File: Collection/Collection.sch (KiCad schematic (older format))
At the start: 3 parts

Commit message: Added power supply schematics to collection.
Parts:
- added C? (x21): C, symbol Device:C
- added D? (x20): D, symbol Device:D
- added L?: FlyBack_Pri_9Winds, symbol Device:L_Core_Ferrite
- added L?: FlyBack_SEC_47Winds_220V, symbol Device:L_Core_Ferrite
- added L?: FlyBack_SEC_13Winds_-100V, symbol Device:L_Core_Ferrite
- added L?: FlyBack_Pri_2-3Winds_6.3VRMS, symbol Device:L_Core_Ferrite
- added L?: FlyBack_Pri_1600Winds_Anode_8-12KV, symbol Device:L_Core_Ferrite
- added L? (x2): Pri_20Winds, symbol Device:L_Core_Ferrite
- added L? (x2): Sec_40Winds, symbol Device:L_Core_Ferrite
- added NE?: Lamp_Neon, symbol Device:Lamp_Neon
- added Q? (x9): Q_NPN, symbol Device:Q_NPN_BCE
- added Q? (x6): Q_PNP, symbol Device:Q_PNP_BCE
- added Q? (x3): Q_NMOS_200V, symbol Device:Q_NMOS_DGS
- added R? (x30): R, symbol Device:R
- added RV? (x3): R_POT, symbol Device:R_POT
- added U1A, U1A?, U1B, U1B?, U1C, U1C?, U1D, U1D?: OPAMP, symbol pspice:OPAMP
- added U? (x2): L7805, symbol Regulator_Linear:L7805
- added U?: 74LS74, symbol 74xx:74LS74
- added U? (x2): 74LS00, symbol 74xx:74LS00
- added U?: L7905, symbol Regulator_Linear:L7905
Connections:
- net +5V: now also C?.1, C?.1, C?.1, C?.1, R?.1, R?.1, R?.1, R?.1, RV?.1, RV?.1, U1A.4 (V+), U1A?.4 (V+), U1B.4 (V+), U1B?.4 (V+), U1C.4 (V+), U1C?.4 (V+), U1D.4 (V+), U1D?.4 (V+), U?.1 (~R), U?.3 (OUT), U?.3 (OUT), U?.4 (~S)
- net CE0 renamed RPI_CE0
- net CE1 renamed RPI_CE1
- net IntensityDAC renamed Intensity_DAC_CE
- net XYdax renamed XY_DAC_CE
- new net: R?.2, R?.2, U1A.2 (-)
- new net: R?.1, R?.2, U1A.3
- new net: D?.1 (K), D?.1 (K), R?.2, U1C.1 (+)
- new net: C?.2, R?.1, U1B.3, U1C.2 (-)
- new net: R?.2, U1C.3
- new net: R?.1, R?.2, U1D.1 (+)
- new net: RV?.2, U1D.2 (-)
- new net: D?.2 (A), U1D.3
- new net: C?.1, R?.1, U1B.2 (-)
- new net: C?.2, D?.2 (A), R?.1, R?.2 (x2)
- new net: Q?.1 (B), R?.1 (x3)
- new net: Q?.1 (B), Q?.1 (B), Q?.2 (C), R?.2 (x3)
- new net: Q?.1 (B), Q?.1 (B), Q?.2 (C), Q?.3 (E) (x3)
- new net: Q?.2 (C), Q?.3 (E), R?.2 (x3)
- new net: L?.2, Q?.1 (D) (x2)
- new net: Q?.2 (G), R?.1 (x3)
- new net: D?.1 (K), D?.2 (A), L?.1, L?.2
- new net: D?.2 (A), L?.1 (x2)
- new net: D?.1 (K), D?.2 (A) (x11)
- new net: C?.1, C?.2
- new net: R?.2, R?.2, U1A?.2 (-)
- new net: R?.1, R?.2, U1A?.3
- new net: C?.2, R?.1, U1B?.3, U1C?.1 (+)
- new net: D?.1 (K), D?.1 (K), R?.2, U1C?.2 (-)
- new net: U1C?.3, U?.1, U?.3 (C), U?.5
- new net: R?.1, R?.2, U1D?.1 (+)
- new net: RV?.2, U1D?.2 (-)
- new net: D?.2 (A), U1D?.3
- new net: C?.1, R?.1, U1B?.2 (-)
- new net: U?.2 (D), U?.4, U?.6 (~Q)
- new net: U?.2, U?.5 (Q)
- new net: R?.2, U?.3
- new net: L?.1, Q?.1 (D)
- new net: R?.2, U?.6
- new net: D?.1 (K), L?.1
- new net +12V: C?.1, C?.1, C?.1, C?.1, L?.1, L?.1, L?.2, Q?.2 (C), Q?.2 (C), Q?.2 (C), Q?.2 (C), Q?.2 (C), Q?.2 (C), R?.1, R?.1, R?.1, U?.1 (IN), U?.1 (IN)
- new net +25V: C?.1, D?.1 (K), R?.1
- new net +2V5: C?.1, C?.1, R?.1, R?.1, R?.2, R?.2, U1A.1 (+), U1A?.1 (+), U1B.1 (+), U1B?.1 (+)
- new net -100V: C?.1, D?.2 (A), R?.2
- new net -25V: C?.1, C?.2, D?.2 (A), U?.2 (VI)
- new net -5V: C?.2, U?.3 (VO)
- new net CRT+220V: C?.1, D?.1 (K), R?.1
- new net CRT_ANODE_8-12KV: C?.1, D?.1 (K)
- new net CRT_GRID: C?.1, NE?.2, R?.1, RV?.1, RV?.2
- new net CRT_Heater2: L?.1
- new net GND: C?.1, C?.1, C?.2, C?.2, C?.2, C?.2, C?.2, C?.2, C?.2, C?.2, C?.2, C?.2, C?.2, C?.2, C?.2, C?.2, L?.1, L?.2, L?.2, L?.2, L?.2, L?.2, NE?.1, Q?.3 (E), Q?.3 (E), Q?.3 (E), Q?.3 (E), Q?.3 (E), Q?.3 (E), Q?.3 (E), Q?.3 (E), Q?.3 (E), Q?.3 (S), Q?.3 (S), Q?.3 (S), R?.1, R?.1, R?.2, R?.2, R?.2, R?.2, R?.2, R?.2, RV?.3, RV?.3, U1A.5 (V-), U1A?.5 (V-), U1B.5 (V-), U1B?.5 (V-), U1C.5 (V-), U1C?.5 (V-), U1D.5 (V-), U1D?.5 (V-), U?.1 (GND), U?.2 (GND), U?.2 (GND)
- new net IntensityCTRL: RV?.3
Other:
- moved on the sheet: U?A, U?B

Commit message: Added Deflection Amp Schematic and Beam Intensity Control Schematic.
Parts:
- added C? (x3): C, symbol Device:C
- added D? (x4): D, symbol Device:D
- added D?: LED, symbol Device:LED
- added L?: X_Deflection, symbol Device:L_Core_Ferrite
- added L?: Y_Deflection, symbol Device:L_Core_Ferrite
- added Q?: Q_PNP_100V, symbol Device:Q_PNP_BCE
- added R? (x17): R, symbol Device:R
- added RV? (x8): R_POT, symbol Device:R_POT
- added U1D? (x6): LM741, symbol pspice:OPAMP
- added U1D? (x2): OPAMP, symbol pspice:OPAMP
- added U? (x2): EL817, Package_DIP:DIP-4_W7.62mm, symbol Isolator:EL817
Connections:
- net +25V: now also U1D?.4 (V+), U1D?.4 (V+)
- net +5V: no longer C?.1, C?.1, R?.1, R?.1, U1A?.4 (V+), U1B?.4 (V+), U1C?.4 (V+), U1D?.4 (V+), U?.3 (OUT), U?.4 (~S)
- net -25V: now also U1D?.5 (V-), U1D?.5 (V-)
- net -5V: now also R?.2, R?.2, U1D?.5 (V-), U1D?.5 (V-), U1D?.5 (V-), U1D?.5 (V-), U1D?.5 (V-), U1D?.5 (V-)
- net GND: now also C?.1, D?.1 (K), L?.2, L?.2, R?.1, R?.1, R?.1, R?.1, R?.1, R?.1, U1D?.2 (-), U1D?.2 (-), U?.1, U?.2, U?.3
- net IntensityCTRL: now also Q?.2 (C)
- new net: R?.2, RV?.3, U1D?.2 (-) (x6)
- new net: C?.1, R?.2, U1D?.1 (+) (x2)
- new net: L?.1, RV?.1, RV?.2, U1D?.3 (x2)
- new net: D?.2 (A), R?.1, RV?.1, RV?.2, U1D?.3 (x2)
- new net: R?.1, R?.2, U1D?.1 (+) (x2)
- new net: D?.2 (A), R?.2, U1D?.3 (x2)
- new net: C?.2, D?.1 (K), D?.1 (K), D?.1 (K), D?.1 (K), RV?.1, RV?.2
- new net: D?.2 (A), R?.2
- new net: R?.1, R?.1, RV?.3
- new net: R?.2, U?.1
- new net: U?.3, U?.4
- new net: Q?.3 (E), U?.4
- new net: R?.1, U?.2
- new net: Q?.1 (B), RV?.2
- new net: R?.1, RV?.3
- new net: R?.1, RV?.1
- new net +5VA: C?.1, C?.1, R?.1, R?.1, U1A?.4 (V+), U1B?.4 (V+), U1C?.4 (V+), U1D?.4 (V+), U1D?.4 (V+), U1D?.4 (V+), U1D?.4 (V+), U1D?.4 (V+), U1D?.4 (V+), U1D?.4 (V+), U?.3 (OUT), U?.4 (~S)
- new net Intensity_From_DAC: R?.2
- new net X_IN: U1D?.1 (+)
- new net X_SIGNAL: C?.2, R?.1, RV?.1, RV?.2, U1D?.1 (+), U1D?.3
- new net Y_IN: U1D?.1 (+)
- new net Y_SIGNAL: C?.2, R?.1, RV?.1, RV?.2, U1D?.1 (+), U1D?.3

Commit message: Updated Op-Amp types on schematics.
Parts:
- added C? (x2): C, symbol Device:C
- added R? (x2): R, symbol Device:R
- U1A, U1A?, U1B, U1B?, U1C, U1C?, U1D, U1D?: value OPAMP -> AD8668
- U1D? (x2): value OPAMP -> LM1875
- U1D? (x4): value LM741 -> LM324
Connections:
- net GND: now also R?.1, R?.1
- net X_SIGNAL: now also C?.2; no longer U1D?.1 (+)
- net Y_SIGNAL: now also C?.2; no longer U1D?.1 (+)
- new net: C?.1, R?.2, U1D?.1 (+) (x2)
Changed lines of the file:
@@
 P 9150 2750
 F 0 "U1A" H 9200 3000 50  0000 L CNN
-F 1 "OPAMP" H 9200 2900 50  0000 L CNN
+F 1 "AD8668" H 9200 2900 50  0000 L CNN
 F 2 "" H 9150 2750 50  0001 C CNN
 F 3 "~" H 9150 2750 50  0001 C CNN
@@
 P 11600 2750
 F 0 "U1C" H 11700 3000 50  0000 L CNN
-F 1 "OPAMP" H 11750 2900 50  0000 L CNN
+F 1 "AD8668" H 11650 2900 50  0000 L CNN
 F 2 "" H 11600 2750 50  0001 C CNN
 F 3 "~" H 11600 2750 50  0001 C CNN
@@
 P 10500 3750
 F 0 "U1D" H 10600 3900 50  0000 L CNN
-F 1 "OPAMP" H 10700 3700 50  0000 L CNN
+F 1 "AD8668" H 10700 3700 50  0000 L CNN
 F 2 "" H 10500 3750 50  0001 C CNN
 F 3 "~" H 10500 3750 50  0001 C CNN
@@
 P 10500 2650
 F 0 "U1B" H 10550 2850 50  0000 L CNN
-F 1 "OPAMP" H 10700 2800 50  0000 L CNN
+F 1 "AD8668" H 10700 2800 50  0000 L CNN
 F 2 "" H 10500 2650 50  0001 C CNN
 F 3 "~" H 10500 2650 50  0001 C CNN
@@
 P 3950 1500
 F 0 "U1B?" H 4000 1700 50  0000 L CNN
-F 1 "OPAMP" H 4150 1650 50  0000 L CNN
+F 1 "AD8668" H 4150 1650 50  0000 L CNN
 F 2 "" H 3950 1500 50  0001 C CNN
 F 3 "~" H 3950 1500 50  0001 C CNN
@@
 P 3950 2600
 F 0 "U1D?" H 4050 2750 50  0000 L CNN
-F 1 "OPAMP" H 4150 2550 50  0000 L CNN
+F 1 "AD8668" H 4150 2550 50  0000 L CNN
 F 2 "" H 3950 2600 50  0001 C CNN
 F 3 "~" H 3950 2600 50  0001 C CNN
@@
 P 5050 1600
 F 0 "U1C?" H 5150 1850 50  0000 L CNN
-F 1 "OPAMP" H 5200 1750 50  0000 L CNN
+F 1 "AD8668" H 5200 1750 50  0000 L CNN
 F 2 "" H 5050 1600 50  0001 C CNN
 F 3 "~" H 5050 1600 50  0001 C CNN
@@
 P 2600 1600
 F 0 "U1A?" H 2650 1850 50  0000 L CNN
-F 1 "OPAMP" H 2650 1750 50  0000 L CNN
+F 1 "AD8668" H 2650 1750 50  0000 L CNN
 F 2 "" H 2600 1600 50  0001 C CNN
 F 3 "~" H 2600 1600 50  0001 C CNN
@@
 P 3400 7900
 F 0 "U1D?" H 3500 8050 50  0000 L CNN
-F 1 "OPAMP" H 3600 7850 50  0000 L CNN
+F 1 "LM1875" H 3500 8150 50  0000 L CNN
 F 2 "" H 3400 7900 50  0001 C CNN
 F 3 "~" H 3400 7900 50  0001 C CNN
@@
 P 3400 9600
 F 0 "U1D?" H 3500 9750 50  0000 L CNN
-F 1 "OPAMP" H 3600 9550 50  0000 L CNN
+F 1 "LM1875" H 3450 9850 50  0000 L CNN
 F 2 "" H 3400 9600 50  0001 C CNN
 F 3 "~" H 3400 9600 50  0001 C CNN
@@
 P 6000 7850
 F 0 "U1D?" H 6100 8000 50  0000 L CNN
-F 1 "LM741" H 6000 8100 50  0000 L CNN
+F 1 "LM324" H 6000 8100 50  0000 L CNN
 F 2 "" H 6000 7850 50  0001 C CNN
 F 3 "~" H 6000 7850 50  0001 C CNN
@@
 P 6000 9550
 F 0 "U1D?" H 6100 9700 50  0000 L CNN
-F 1 "LM741" H 6050 9800 50  0000 L CNN
+F 1 "LM324" H 6050 9800 50  0000 L CNN
 F 2 "" H 6000 9550 50  0001 C CNN
 F 3 "~" H 6000 9550 50  0001 C CNN
@@
 P 7250 7950
 F 0 "U1D?" H 7350 8100 50  0000 L CNN
-F 1 "LM741" H 7250 8200 50  0000 L CNN
+F 1 "LM324" H 7250 8200 50  0000 L CNN
 F 2 "" H 7250 7950 50  0001 C CNN
 F 3 "~" H 7250 7950 50  0001 C CNN
@@
 P 7250 9650
 F 0 "U1D?" H 7350 9800 50  0000 L CNN
-F 1 "LM741" H 7250 9900 50  0000 L CNN
+F 1 "LM324" H 7250 9900 50  0000 L CNN
 F 2 "" H 7250 9650 50  0001 C CNN
 F 3 "~" H 7250 9650 50  0001 C CNN
@@
 Text GLabel 8450 7250 0    50   Input ~ 0
 Intensity_Control
-Text Label 5200 7650 0    50   ~ 0
+Text Label 5200 7350 0    50   ~ 0
 X_SIGNAL
-Text Label 5200 9350 0    50   ~ 0
+Text Label 5200 9050 0    50   ~ 0
 Y_SIGNAL
+$Comp
+L Device:C C?
+U 1 1 643A120E
+P 5350 7750
+F 0 "C?" V 5050 7750 50  0000 C CNN
+F 1 "C" V 5150 7750 50  0000 C CNN
+F 2 "" H 5388 7600 50  0001 C CNN
+F 3 "~" H 5350 7750 50  0001 C CNN
+	1    5350 7750
+	0    1    1    0
+$EndComp
+$Comp
+L Device:C C?
+U 1 1 643A1B0E
+P 5350 9450
+F 0 "C?" V 5050 9450 50  0000 C CNN
+F 1 "C" V 5150 9450 50  0000 C CNN
+F 2 "" H 5388 9300 50  0001 C CNN
+F 3 "~" H 5350 9450 50  0001 C CNN
+	1    5350 9450
+	0    1    1    0
+$EndComp
+Wire Wire Line
+	5200 7350 5200 7750
+Wire Wire Line
+	5500 7750 5700 7750
 Wire Wire Line
-	5200 7750 5200 7650
+	5200 9050 5200 9450
 Wire Wire Line
-	5200 7750 5700 7750
+	5500 9450 5700 9450
+$Comp
+L Device:R R?
+U 1 1 6440C003
+P 5500 8100
+F 0 "R?" H 5400 8050 50  0000 R CNN
+F 1 "R" H 5400 8100 50  0000 R CNN
+F 2 "" V 5430 8100 50  0001 C CNN
+F 3 "~" H 5500 8100 50  0001 C CNN
+	1    5500 8100
+	-1   0    0    1
+$EndComp
+$Comp
+L power:GND #PWR?
+U 1 1 6440D5EB
+P 5500 8250
+F 0 "#PWR?" H 5500 8000 50  0001 C CNN
+F 1 "GND" H 5550 8050 50  0000 C CNN
+F 2 "" H 5500 8250 50  0001 C CNN
+F 3 "" H 5500 8250 50  0001 C CNN
+	1    5500 8250
+	1    0    0    -1
+$EndComp
+$Comp
+L Device:R R?
+U 1 1 64426FB5
+P 5500 9800
+F 0 "R?" H 5400 9750 50  0000 R CNN
+F 1 "R" H 5400 9800 50  0000 R CNN
+F 2 "" V 5430 9800 50  0001 C CNN
+F 3 "~" H 5500 9800 50  0001 C CNN
+	1    5500 9800
+	-1   0    0    1
+$EndComp
+$Comp
+L power:GND #PWR?
+U 1 1 644285B9
+P 5500 9950
+F 0 "#PWR?" H 5500 9700 50  0001 C CNN
+F 1 "GND" H 5550 9750 50  0000 C CNN
+F 2 "" H 5500 9950 50  0001 C CNN
+F 3 "" H 5500 9950 50  0001 C CNN
+	1    5500 9950
+	1    0    0    -1
+$EndComp
 Wire Wire Line
-	5200 9450 5200 9350
+	5500 9650 5500 9450
+Connection ~ 5500 9450
 Wire Wire Line
-	5200 9450 5700 9450
+	5500 7950 5500 7750
+Connection ~ 5500 7750
 $EndSCHEMATC

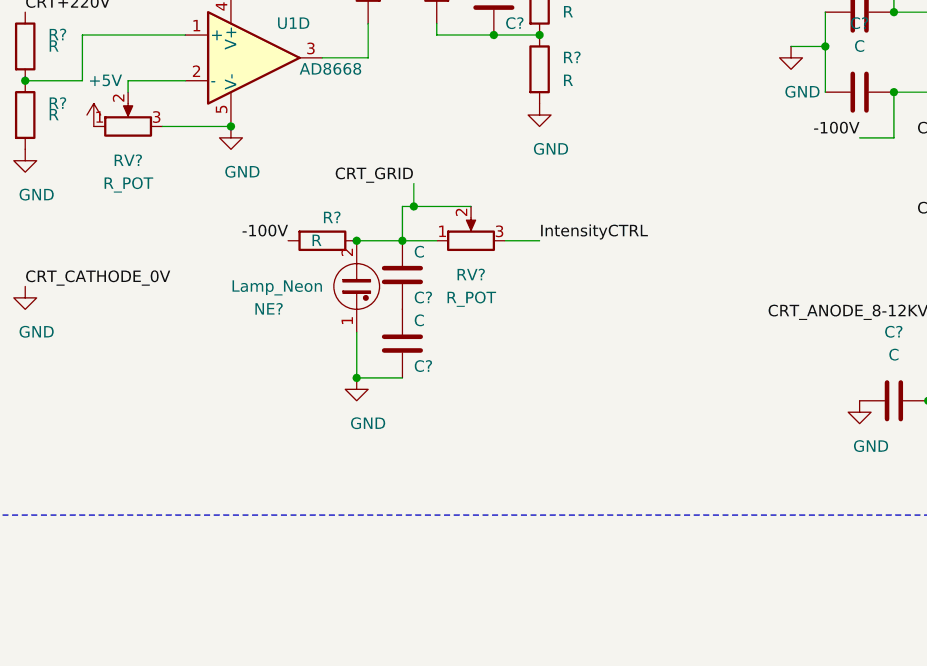
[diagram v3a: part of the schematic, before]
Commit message: Updated Intensity control Circuit.
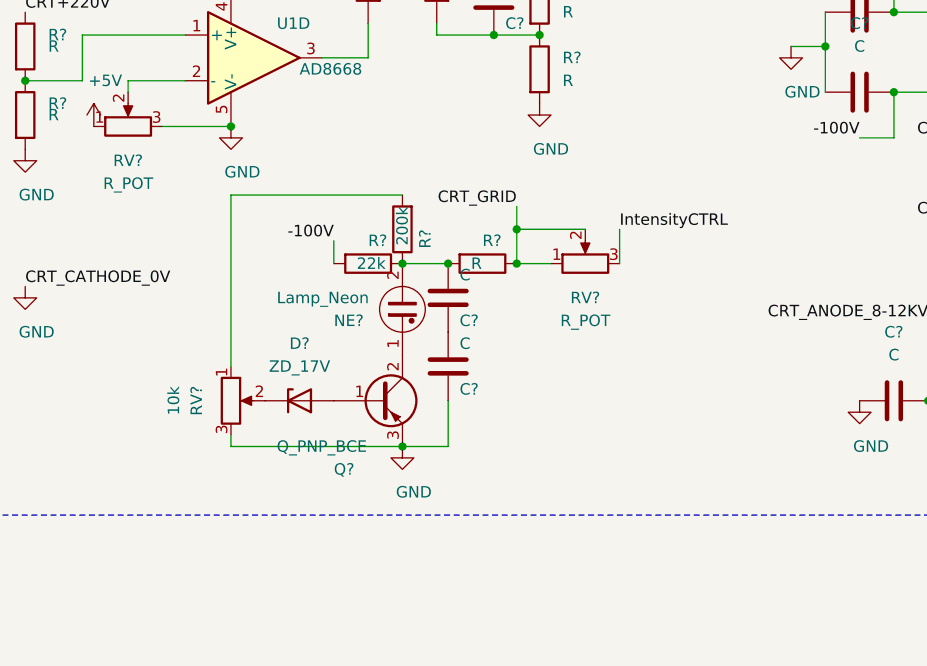
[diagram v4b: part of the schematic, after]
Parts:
- added D?: ZD_17V, symbol Device:D_Zener
- added Q?: Q_PNP_BCE, symbol Device:Q_PNP_BCE
- added R?: R, symbol Device:R
- added R?: 200k, symbol Device:R
- added RV?: 10k, symbol Device:R_POT
- R?: value R -> 22k
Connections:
- net CRT_GRID: now also R?.1; no longer C?.1, NE?.2, R?.1
- net GND: now also Q?.3 (E), RV?.3; no longer NE?.1
- new net: C?.1, NE?.2, R?.1, R?.1, R?.2
- new net: NE?.1, Q?.2 (C)
- new net: D?.2 (A), Q?.1 (B)
- new net: D?.1 (K), RV?.2
- new net: R?.2, RV?.1
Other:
- moved on the sheet: C?, NE?, R?, RV?
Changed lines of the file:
@@
 Wire Wire Line
 	14650 2400 14750 2400
-Text Label 10650 4550 2    50   ~ 0
+Text Label 10850 4550 2    50   ~ 0
 -100V
 $Comp
 L Device:Lamp_Neon NE?
 U 1 1 64460D5E
-P 10950 4750
-F 0 "NE?" H 10500 4650 50  0000 L CNN
-F 1 "Lamp_Neon" H 10400 4750 50  0000 L CNN
-F 2 "" V 10950 4850 50  0001 C CNN
-F 3 "~" V 10950 4850 50  0001 C CNN
-	1    10950 4750
+P 11150 4850
+F 0 "NE?" H 10850 4800 50  0000 L CNN
+F 1 "Lamp_Neon" H 10600 4900 50  0000 L CNN
+F 2 "" V 11150 4950 50  0001 C CNN
+F 3 "~" V 11150 4950 50  0001 C CNN
+	1    11150 4850
 	1    0    0    -1
 $EndComp
@@
 L Device:R R?
 U 1 1 644615DC
-P 10800 4550
-F 0 "R?" V 10700 4550 50  0000 L CNN
-F 1 "R" V 10800 4500 50  0000 L CNN
-F 2 "" V 10730 4550 50  0001 C CNN
-F 3 "~" H 10800 4550 50  0001 C CNN
-	1    10800 4550
+P 11000 4650
+F 0 "R?" V 10900 4650 50  0000 L CNN
+F 1 "22k" V 11000 4600 50  0000 L CNN
+F 2 "" V 10930 4650 50  0001 C CNN
+F 3 "~" H 11000 4650 50  0001 C CNN
+	1    11000 4650
 	0    1    1    0
 $EndComp
@@
 L power:GND #PWR?
 U 1 1 644620C7
-P 10950 5150
-F 0 "#PWR?" H 10950 4900 50  0001 C CNN
-F 1 "GND" H 11000 4950 50  0000 C CNN
-F 2 "" H 10950 5150 50  0001 C CNN
-F 3 "" H 10950 5150 50  0001 C CNN
-	1    10950 5150
+P 11150 5450
+F 0 "#PWR?" H 11150 5200 50  0001 C CNN
+F 1 "GND" H 11200 5250 50  0000 C CNN
+F 2 "" H 11150 5450 50  0001 C CNN
+F 3 "" H 11150 5450 50  0001 C CNN
+	1    11150 5450
 	1    0    0    -1
 $EndComp
@@
 L Device:C C?
 U 1 1 64462CFE
-P 11150 4700
-F 0 "C?" H 11200 4600 50  0000 L CNN
-F 1 "C" H 11200 4800 50  0000 L CNN
-F 2 "" H 11188 4550 50  0001 C CNN
-F 3 "~" H 11150 4700 50  0001 C CNN
-	1    11150 4700
+P 11350 4800
+F 0 "C?" H 11400 4700 50  0000 L CNN
+F 1 "C" H 11400 4900 50  0000 L CNN
+F 2 "" H 11388 4650 50  0001 C CNN
+F 3 "~" H 11350 4800 50  0001 C CNN
+	1    11350 4800
 	1    0    0    -1
 $EndComp
@@
 L Device:C C?
 U 1 1 6446347D
-P 11150 5000
-F 0 "C?" H 11200 4900 50  0000 L CNN
-F 1 "C" H 11200 5100 50  0000 L CNN
-F 2 "" H 11188 4850 50  0001 C CNN
-F 3 "~" H 11150 5000 50  0001 C CNN
-	1    11150 5000
-	1    0    0    -1
-$EndComp
-Wire Wire Line
-	11150 5150 10950 5150
-Wire Wire Line
-	10950 5150 10950 4950
-Connection ~ 10950 5150
-Wire Wire Line
-	10950 4550 11150 4550
-Connection ~ 10950 4550
+P 11350 5100
+F 0 "C?" H 11400 5000 50  0000 L CNN
+F 1 "C" H 11400 5200 50  0000 L CNN
+F 2 "" H 11388 4950 50  0001 C CNN
+F 3 "~" H 11350 5100 50  0001 C CNN
+	1    11350 5100
+	1    0    0    -1
+$EndComp
+Wire Wire Line
+	11150 4650 11350 4650
 $Comp
 L Device:R_POT RV?
 U 1 1 6446BA10
-P 11450 4550
-F 0 "RV?" V 11300 4550 50  0000 C CNN
-F 1 "R_POT" V 11200 4550 50  0000 C CNN
-F 2 "" H 11450 4550 50  0001 C CNN
-F 3 "~" H 11450 4550 50  0001 C CNN
-	1    11450 4550
+P 11950 4650
+F 0 "RV?" V 11800 4650 50  0000 C CNN
+F 1 "R_POT" V 11700 4650 50  0000 C CNN
+F 2 "" H 11950 4650 50  0001 C CNN
+F 3 "~" H 11950 4650 50  0001 C CNN
+	1    11950 4650
 	0    -1   -1   0
 $EndComp
 Wire Wire Line
-	11300 4550 11150 4550
-Connection ~ 11150 4550
-Wire Wire Line
-	11150 4550 11150 4400
-Wire Wire Line
-	11150 4400 11200 4400
-Text Label 11200 4300 2    50   ~ 0
+	11800 4650 11650 4650
+Connection ~ 11350 4650
+Text Label 11650 4400 2    50   ~ 0
 CRT_GRID
-Wire Wire Line
-	11200 4300 11200 4400
-Connection ~ 11200 4400
-Wire Wire Line
-	11200 4400 11450 4400
-Text Label 11750 4550 0    50   ~ 0
-IntensityCTRL
-Wire Wire Line
-	11750 4550 11600 4550
 Wire Notes Line
 	15600 5750 7950 5750
@@
 	5500 7950 5500 7750
 Connection ~ 5500 7750
+Text Label 12100 4500 0    50   ~ 0
+IntensityCTRL
+$Comp
+L Device:R R?
+U 1 1 6442BE8E
+P 11500 4650
+F 0 "R?" V 11400 4650 50  0000 L CNN
+F 1 "R" V 11500 4600 50  0000 L CNN
+F 2 "" V 11430 4650 50  0001 C CNN
+F 3 "~" H 11500 4650 50  0001 C CNN
+	1    11500 4650
+	0    1    1    0
+$EndComp
+Wire Wire Line
+	11650 4500 11650 4650
+Wire Wire Line
+	11650 4500 11950 4500
+Connection ~ 11650 4650
+Wire Wire Line
+	11650 4400 11650 4500
+Connection ~ 11650 4500
+Wire Wire Line
+	12100 4500 12100 4650
+$Comp
+L Device:Q_PNP_BCE Q?
+U 1 1 64495F1E
+P 11050 5250
+F 0 "Q?" H 10850 4950 50  0000 L CNN
+F 1 "Q_PNP_BCE" H 10600 5050 50  0000 L CNN
+F 2 "" H 11250 5350 50  0001 C CNN
+F 3 "~" H 11050 5250 50  0001 C CNN
+	1    11050 5250
+	1    0    0    -1
+$EndComp
+Connection ~ 11150 4650
+Wire Wire Line
+	11350 5250 11350 5450
+Wire Wire Line
+	11350 5450 11150 5450
+Connection ~ 11150 5450
+$Comp
+L Device:D_Zener D?
+U 1 1 644B4D2D
+P 10700 5250
+F 0 "D?" H 10700 5500 50  0000 C CNN
+F 1 "ZD_17V" H 10700 5400 50  0000 C CNN
+F 2 "" H 10700 5250 50  0001 C CNN
+F 3 "~" H 10700 5250 50  0001 C CNN
+	1    10700 5250
+	1    0    0    -1
+$EndComp
+Wire Wire Line
+	10850 4550 10850 4650
+$Comp
+L Device:R R?
+U 1 1 644EEF86
+P 11150 4500
+F 0 "R?" V 11050 4500 50  0000 L CNN
+F 1 "200k" V 11150 4400 50  0000 L CNN
+F 2 "" V 11080 4500 50  0001 C CNN
+F 3 "~" H 11150 4500 50  0001 C CNN
+	1    11150 4500
+	-1   0    0    1
+$EndComp
+$Comp
+L Device:R_POT RV?
+U 1 1 644F0E02
+P 10400 5250
+F 0 "RV?" V 10250 5250 50  0000 C CNN
+F 1 "10k" V 10150 5250 50  0000 C CNN
+F 2 "" H 10400 5250 50  0001 C CNN
+F 3 "~" H 10400 5250 50  0001 C CNN
+	1    10400 5250
+	1    0    0    -1
+$EndComp
+Wire Wire Line
+	11150 5450 10400 5450
+Wire Wire Line
+	10400 5450 10400 5400
+Wire Wire Line
+	10400 5100 10400 4350
+Wire Wire Line
+	10400 4350 11150 4350
 $EndSCHEMATC

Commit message: Updated schematic. Resistors values are NOT all correct yet.
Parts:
- removed R? (x48): R, symbol Device:R
- added R? (x47): 10K, Resistors_SMD:R_0603, symbol Device:R
- added R?: 870K, Resistors_SMD:R_0603, symbol Device:R
- R?: value R -> 180K; footprint (none) -> Resistors_SMD:R_0603
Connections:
- net +12V: now also R?.1, R?.1, R?.1
- net +2V5: now also R?.1, R?.1, R?.2, R?.2
- net +5V: now also R?.1, R?.1
- net +5VA: now also R?.1, R?.1
- net -5V: now also R?.2, R?.2
- net CRT+220V: now also R?.1
- net CRT_GRID: now also R?.2
- net GND: now also R?.1, R?.1, R?.2, R?.2, R?.2, R?.2, R?.2, R?.2, R?.2, R?.2, R?.2, R?.2, R?.2, R?.2, R?.2, R?.2
- net Intensity_From_DAC: now also R?.2
- net X_SIGNAL: now also R?.1
- net Y_SIGNAL: now also R?.1
- net at U1A.2 (-): now also R?.1, R?.2
- net at U1A.3: now also R?.1, R?.1
- net at D?.1 (K), D?.1 (K), U1C.1 (+): now also R?.2
- net at C?.2, U1B.3, U1C.2 (-): now also R?.2
- net at U1C.3: now also R?.1
- net at U1D.1 (+): now also R?.1, R?.2
- net at C?.1, U1B.2 (-): now also R?.2
- net at C?.2, D?.2 (A): now also R?.1, R?.2 (x2)
- net at C?.1, U1D?.1 (+): now also R?.1 (x2)
- net at Q?.1 (B): now also R?.2 (x3)
- net at Q?.1 (B), Q?.1 (B), Q?.2 (C): now also R?.2 (x3)
- net at Q?.2 (C), Q?.3 (E): now also R?.1 (x3)
- net at Q?.2 (G): now also R?.2 (x3)
- net at D?.2 (A), L?.1: no longer D?.1 (K), L?.2
- net at C?.1, NE?.2, R?.1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: now also R?.1
- net at U1A?.2 (-): now also R?.1, R?.2
- net at U1A?.3: now also R?.1, R?.1
- net at C?.2, U1B?.3, U1C?.1 (+): now also R?.2
- net at D?.1 (K), D?.1 (K), U1C?.2 (-): now also R?.2
- net at R?.2, U1D?.1 (+): now also R?.1
- net at C?.1, U1B?.2 (-): now also R?.2
- net at U?.3: now also R?.1
- net at U?.6: now also R?.1
- net at RV?.3, U1D?.2 (-): now also R?.1 (x6)
- net X_Bypass: now reaches C?.1, U1D?.1 (+)
- net X_Bypass: now also R?.2
- net Y_Bypass: now reaches C?.1, U1D?.1 (+)
- net Y_Bypass: now also R?.2
- net at D?.2 (A), RV?.1, RV?.2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: now also R?.2 (x2)
- net at U1D?.1 (+): now also R?.1, R?.1 (x2)
- net at D?.2 (A), U1D?.3: now also R?.2 (x2)
- net at D?.2 (A): now also R?.2
- net at RV?.3: now also R?.1, R?.1
- net at U?.1: now also R?.2
- net at U?.2: now also R?.1
- net at RV?.3: now also R?.1
- net at RV?.1: now also R?.1
- new net: D?.1 (K), L?.2
